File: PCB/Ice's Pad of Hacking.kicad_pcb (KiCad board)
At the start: 2 copper layers, 80.3 x 100 mm, 53 parts, among them SW1 RotaryEncoder_Switch, SW10 SW_Push, SW11 SW_Push, SW12 SW_Push, SW13 SW_Push, SW14 SW_Push, SW15 SW_Push, SW16 SW_Push, SW17 SW_Push, SW18 SW_Push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

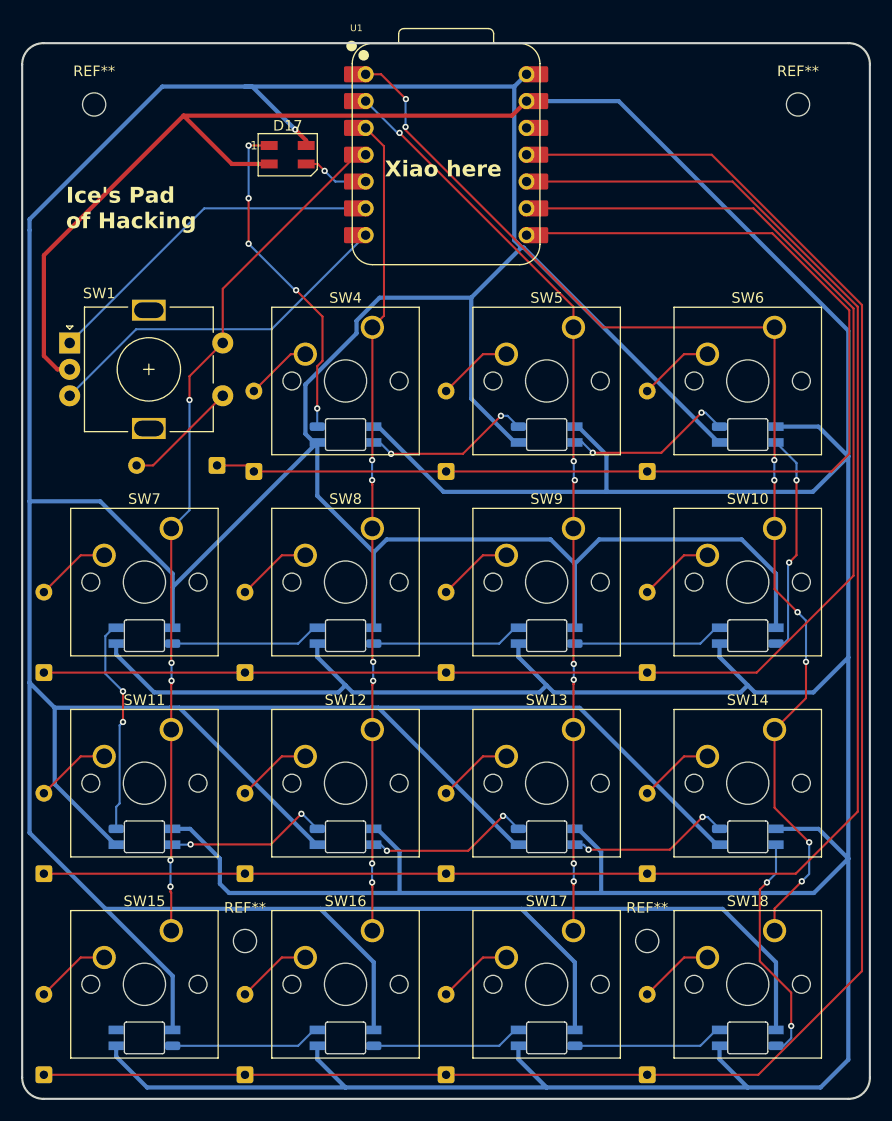
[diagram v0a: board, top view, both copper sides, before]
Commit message: Update PCB mounting hole silkscreen
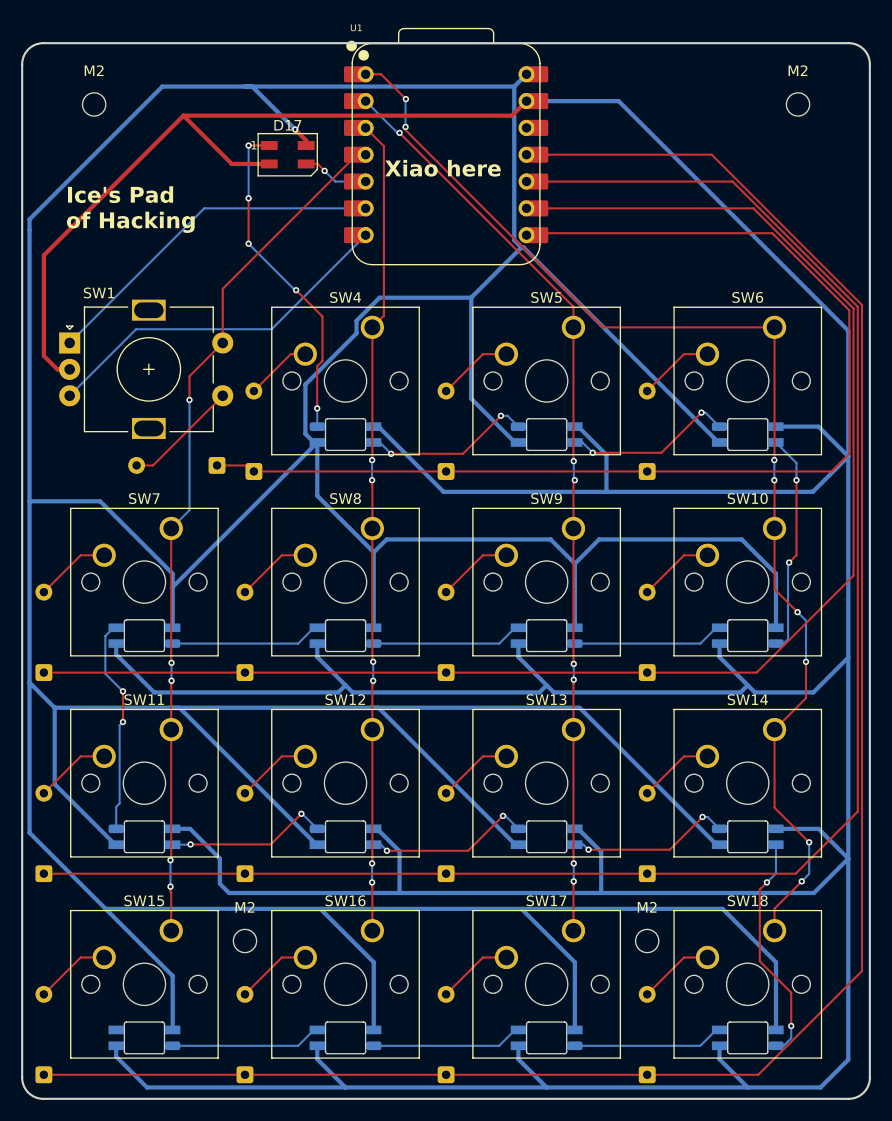
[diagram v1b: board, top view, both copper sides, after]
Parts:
- renumbered REF** to M2
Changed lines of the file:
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@@
 		(descr "Mounting Hole 2.2mm, M2, no annular, generated by kicad-footprint-generator mountinghole.py")
 		(tags "mountinghole M2")
-		(property "Reference" "REF**"
+		(property "Reference" "M2"
 			(at 0 -3.15 0)
 			(layer "F.SilkS")
@@
 		(descr "Mounting Hole 2.2mm, M2, no annular, generated by kicad-footprint-generator mountinghole.py")
 		(tags "mountinghole M2")
-		(property "Reference" "REF**"
+		(property "Reference" "M2"
 			(at 0 -3.15 0)
 			(layer "F.SilkS")
@@
 		(descr "Mounting Hole 2.2mm, M2, no annular, generated by kicad-footprint-generator mountinghole.py")
 		(tags "mountinghole M2")
-		(property "Reference" "REF**"
+		(property "Reference" "M2"
 			(at 0 -3.15 0)
 			(layer "F.SilkS")
@@
 		(descr "Mounting Hole 2.2mm, M2, no annular, generated by kicad-footprint-generator mountinghole.py")
 		(tags "mountinghole M2")
-		(property "Reference" "REF**"
+		(property "Reference" "M2"
 			(at 0 -3.15 0)
 			(layer "F.SilkS")
